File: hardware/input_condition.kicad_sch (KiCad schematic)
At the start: 20 parts

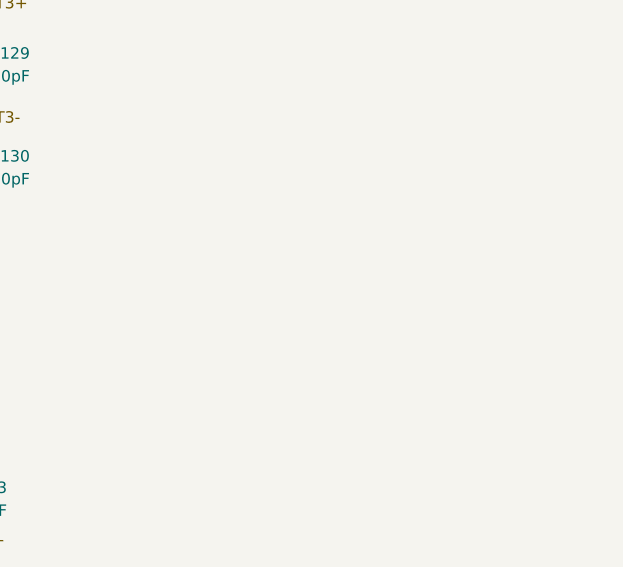
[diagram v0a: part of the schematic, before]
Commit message: feat：电平触发原理图
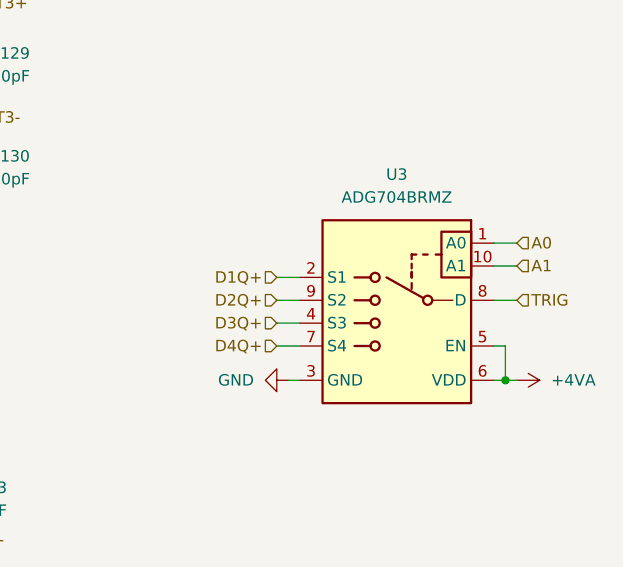
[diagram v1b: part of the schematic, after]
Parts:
- added U3: ADG704BRMZ, Package_SO:TSSOP-10_3x3mm_P0.5mm, symbol Analog_Switch:ADG704BRMZ
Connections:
- net D1Q+: now also U3.2 (S1)
- net D2Q+: now also U3.9 (S2)
- net D3Q+: now also U3.4 (S3)
- net D4Q+: now also U3.7 (S4)
- net GND: now also U3.3 (GND)
- new net +4VA: U3.5 (EN), U3.6 (VDD)
- new net A0: U3.1 (A0)
- new net A1: U3.10 (A1)
- new net TRIG: U3.8 (D)

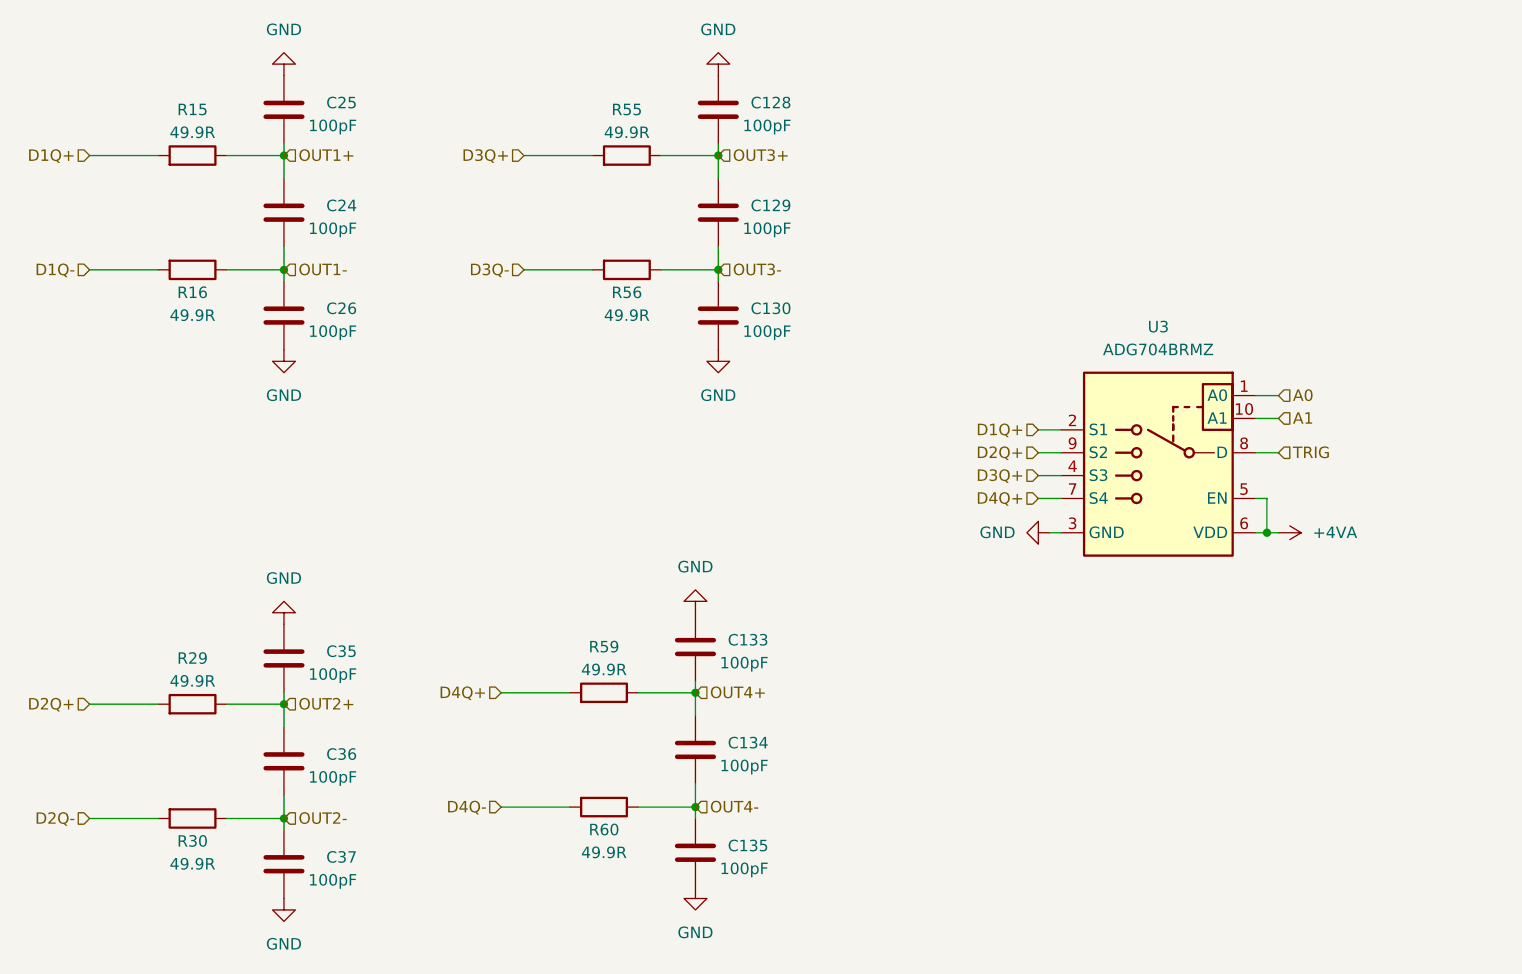
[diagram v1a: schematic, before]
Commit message: feat：电平触发原理图
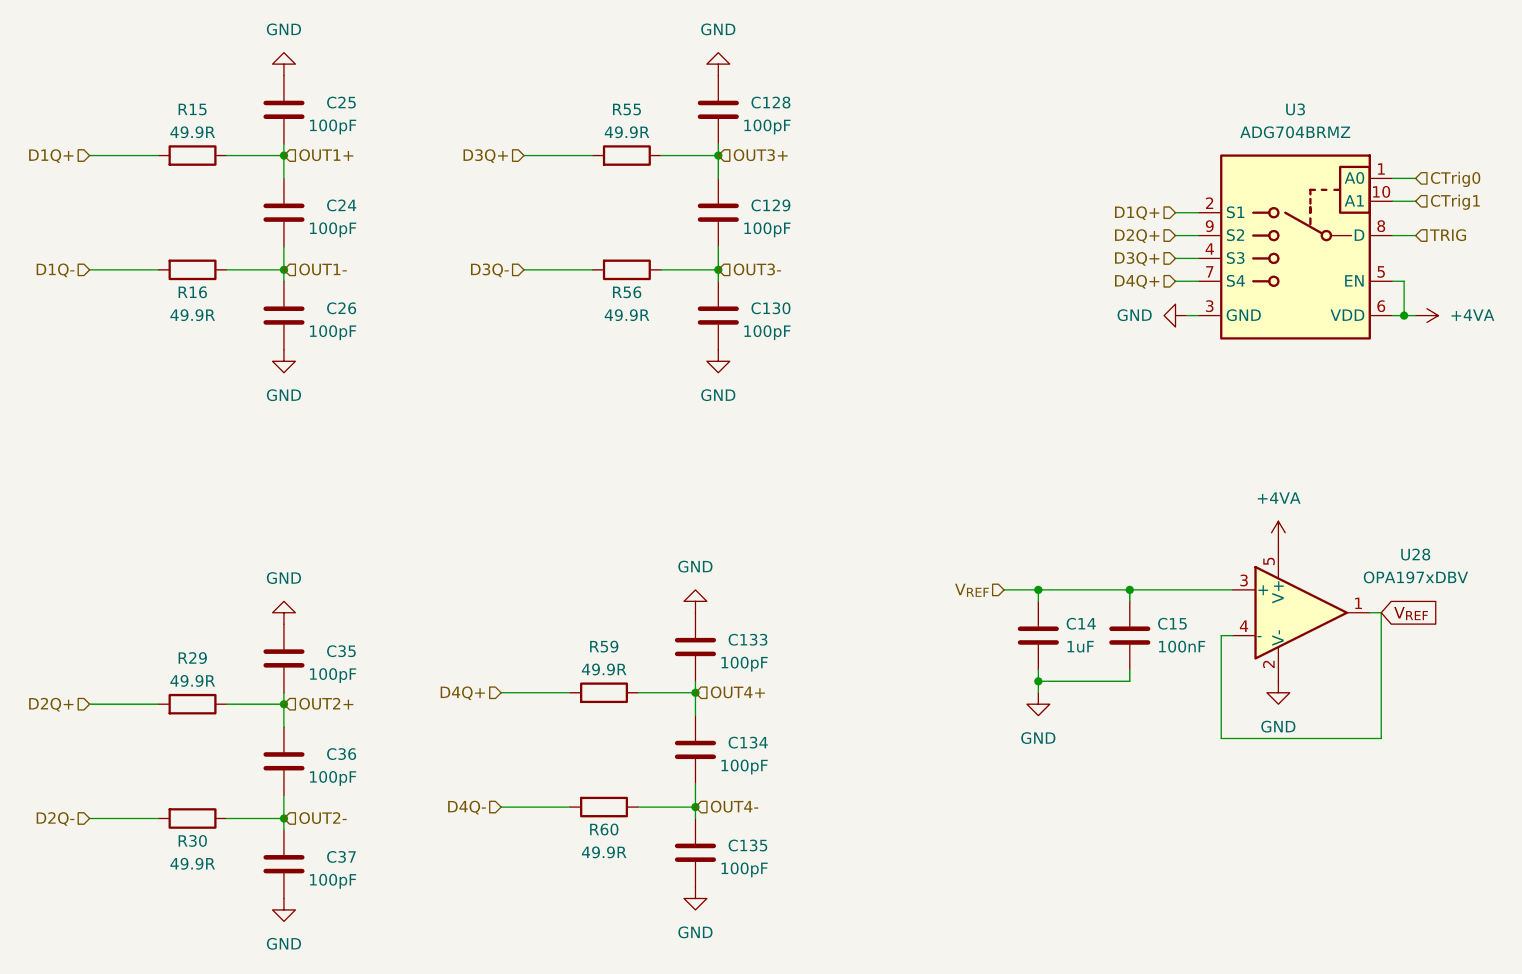
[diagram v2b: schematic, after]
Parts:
- added C14: 1uF, Capacitor_SMD:C_0603_1608Metric, symbol Device:C
- added C15: 100nF, Capacitor_SMD:C_0603_1608Metric, symbol Device:C
- added U28: OPA197xDBV, Package_TO_SOT_SMD:SOT-23-5, symbol Amplifier_Operational:OPA192xDBV
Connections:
- net +4VA: now also U28.5 (V+)
- net GND: now also C14.2, C15.2, U28.2 (V-)
- net A0 renamed CTrig0
- net A1 renamed CTrig1
- new net V_{REF}: C14.1, C15.1, U28.1, U28.3 (+), U28.4 (-)
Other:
- moved on the sheet: U3

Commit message: feat：电源原理图
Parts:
- removed C14: 1uF, Capacitor_SMD:C_0603_1608Metric, symbol Device:C
- removed C15: 100nF, Capacitor_SMD:C_0603_1608Metric, symbol Device:C
- removed U28: OPA197xDBV, Package_TO_SOT_SMD:SOT-23-5, symbol Amplifier_Operational:OPA192xDBV

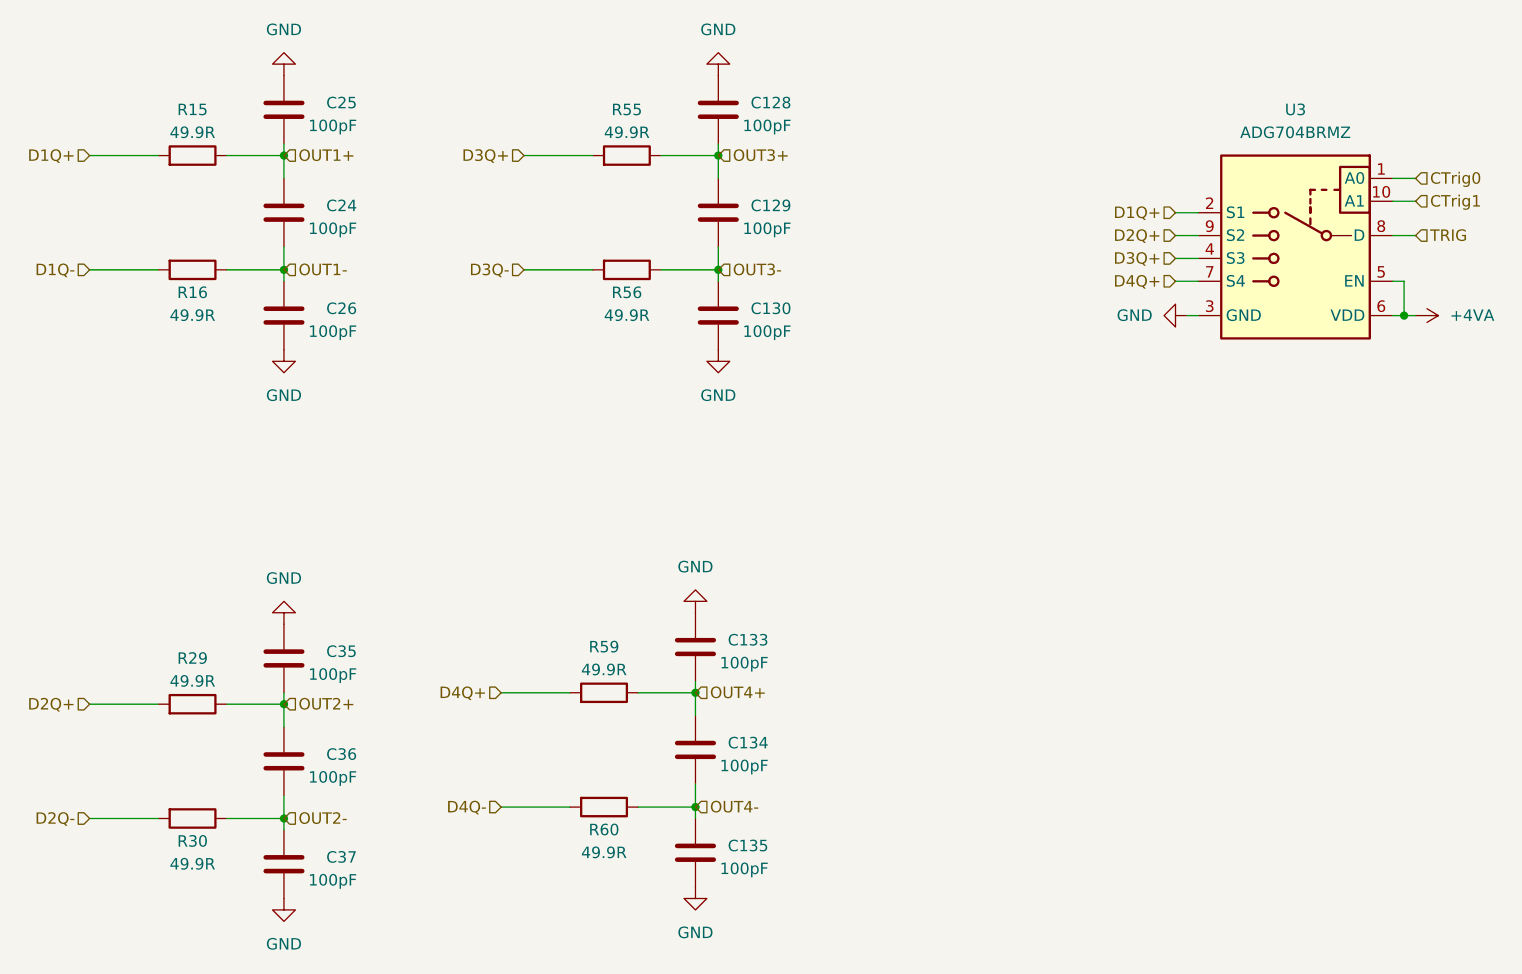
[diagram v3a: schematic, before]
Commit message: feat：模拟前端布线，单片机/SRAM布线
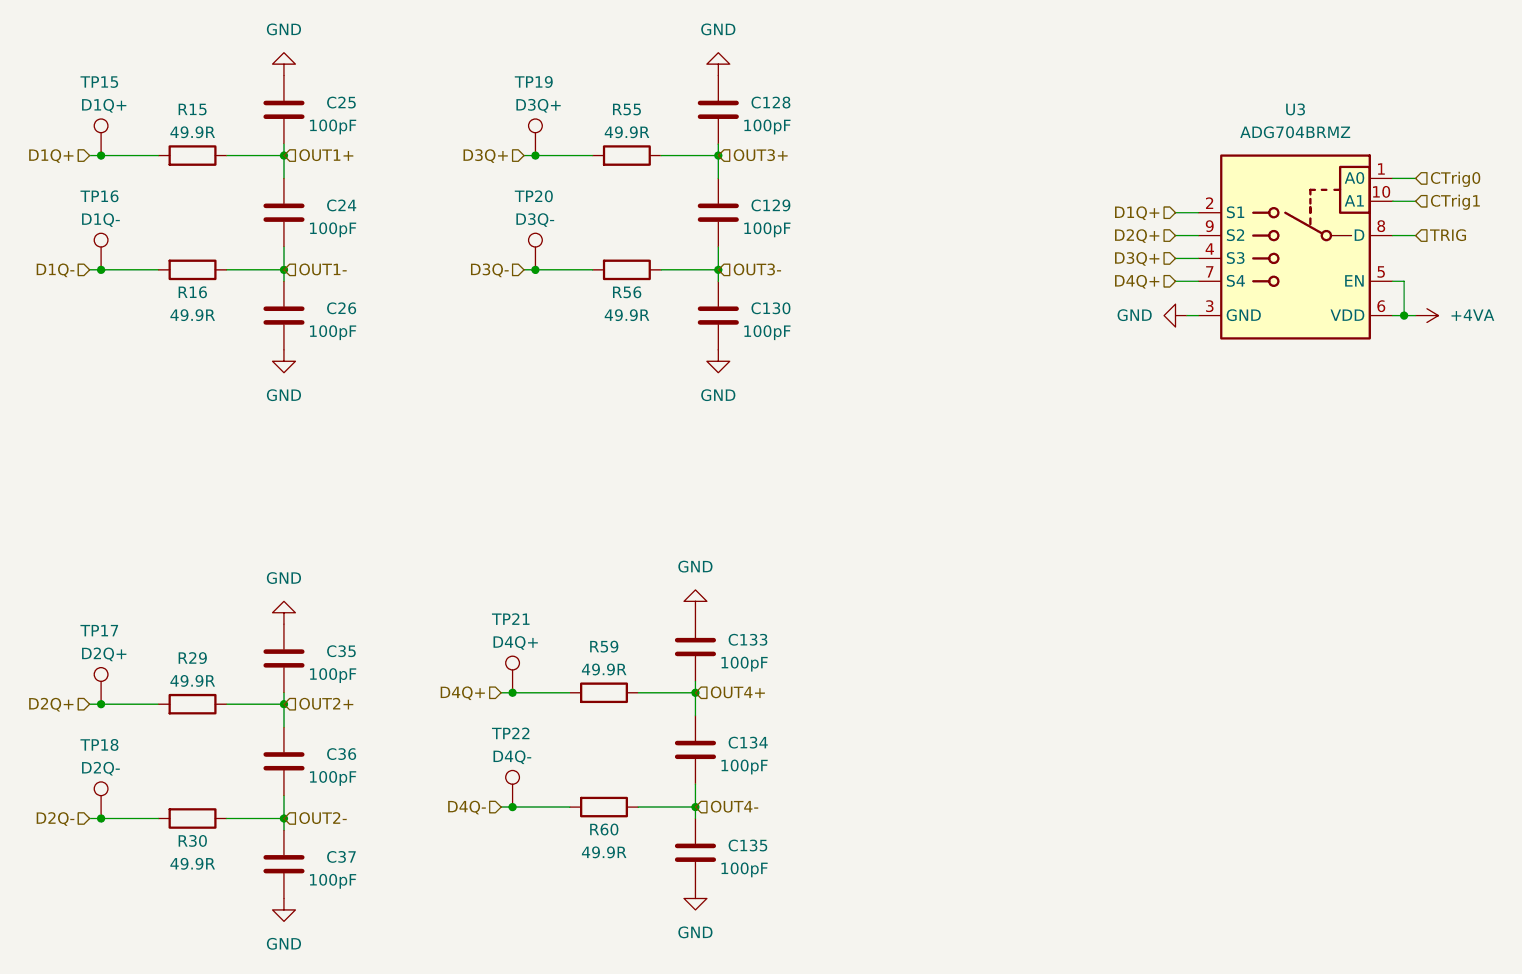
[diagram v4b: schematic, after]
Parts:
- added TP15: D1Q+, TestPoint:TestPoint_Pad_D1.0mm, symbol Connector:TestPoint
- added TP16: D1Q-, TestPoint:TestPoint_Pad_D1.0mm, symbol Connector:TestPoint
- added TP17: D2Q+, TestPoint:TestPoint_Pad_D1.0mm, symbol Connector:TestPoint
- added TP18: D2Q-, TestPoint:TestPoint_Pad_D1.0mm, symbol Connector:TestPoint
- added TP19: D3Q+, TestPoint:TestPoint_Pad_D1.0mm, symbol Connector:TestPoint
- added TP20: D3Q-, TestPoint:TestPoint_Pad_D1.0mm, symbol Connector:TestPoint
- added TP21: D4Q+, TestPoint:TestPoint_Pad_D1.0mm, symbol Connector:TestPoint
- added TP22: D4Q-, TestPoint:TestPoint_Pad_D1.0mm, symbol Connector:TestPoint
- C128, C129, C130, C133, C134, C135, C24, C25, C26, C35, C36, C37: footprint Capacitor_SMD:C_0603_1608Metric -> Capacitor_SMD:C_0402_1005Metric
- R15, R16, R29, R30, R55, R56, R59, R60: footprint Resistor_SMD:R_0603_1608Metric -> Resistor_SMD:R_0402_1005Metric
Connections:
- net D1Q+: now also TP15.1
- net D1Q-: now also TP16.1
- net D2Q+: now also TP17.1
- net D2Q-: now also TP18.1
- net D3Q+: now also TP19.1
- net D3Q-: now also TP20.1
- net D4Q+: now also TP21.1
- net D4Q-: now also TP22.1
